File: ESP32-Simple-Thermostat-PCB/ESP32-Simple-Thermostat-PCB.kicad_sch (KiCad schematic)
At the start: 47 parts, among them J1 PINHD_1x18_Male, J2 Screw_Terminal_9_P3.50mm, J3 DS18B20, J4 3.2 lcd tft, K1 G5Q-1A, K2 G5Q-1A, K3 G5Q-1A, K4 G5Q-1A, K5 G5Q-1A, K6 G5Q-1A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

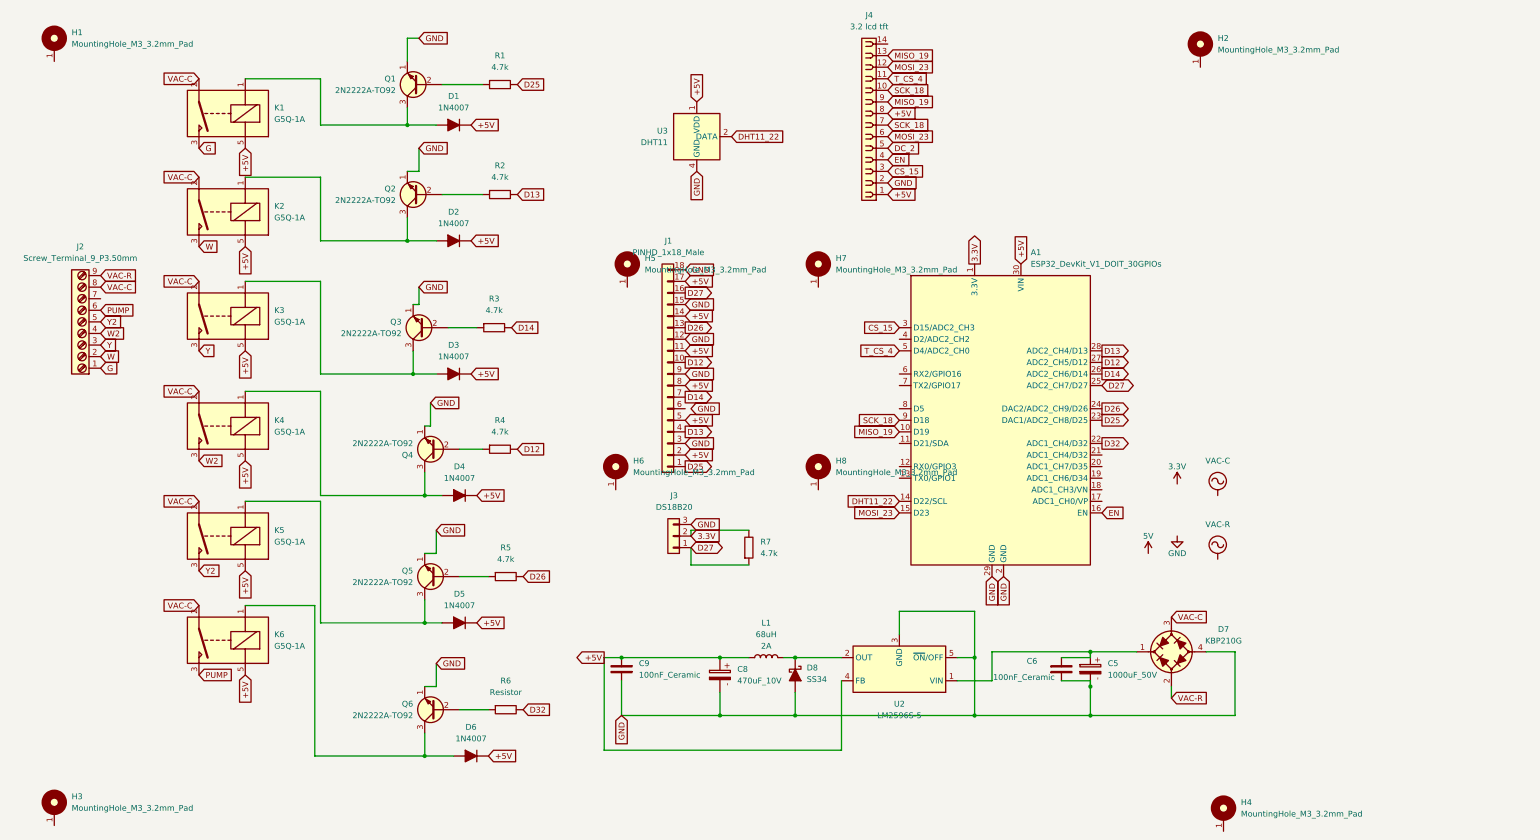
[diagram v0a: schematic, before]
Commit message: Standardize project naming to ESP32 Simple Thermostat
- Updated display text, serial messages, and MQTT device model
- Updated all web interface page titles and headers
- Consistent branding across documentation and code
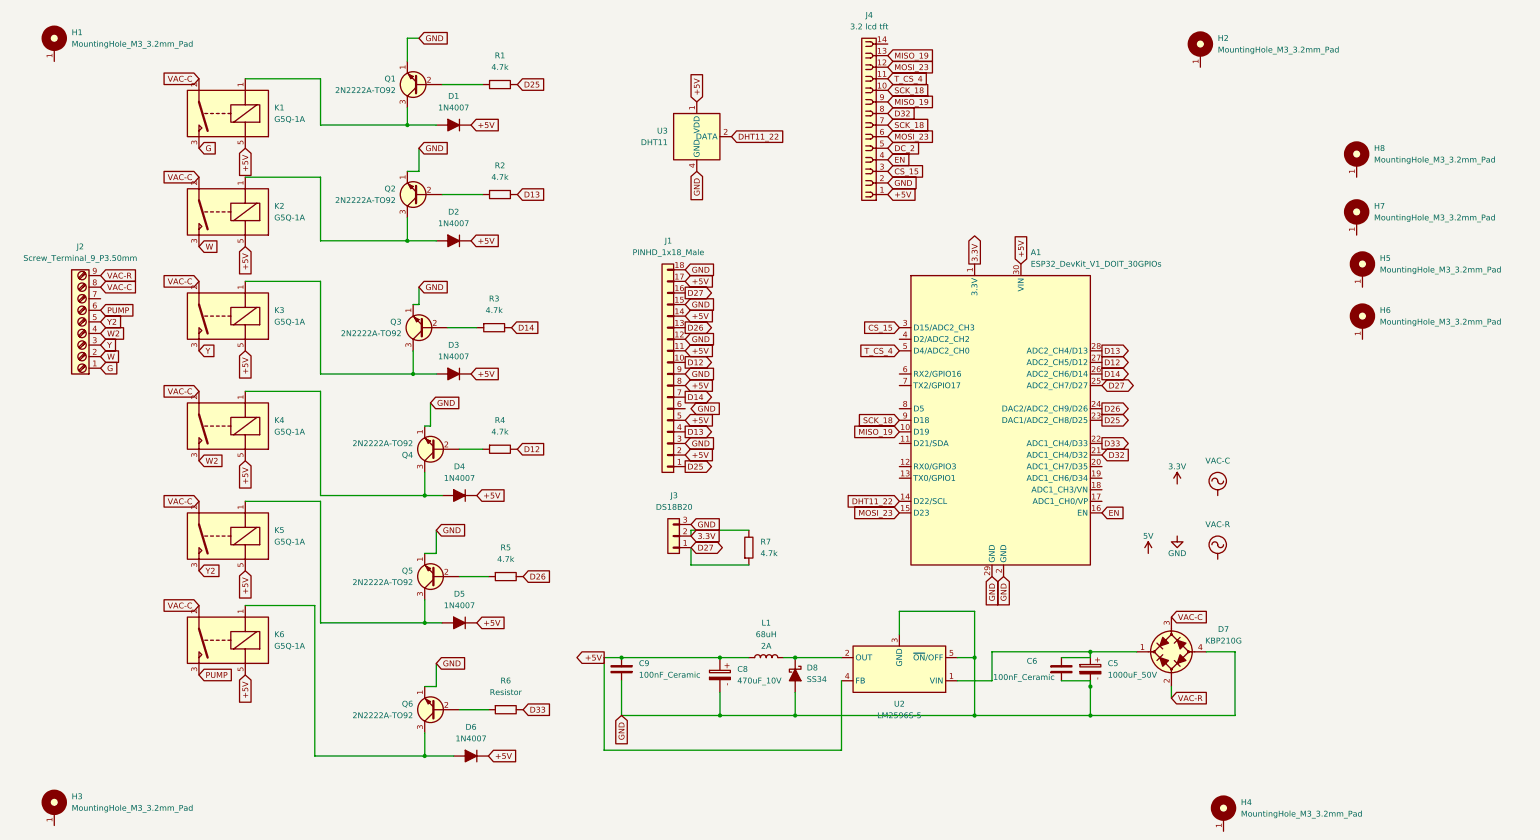
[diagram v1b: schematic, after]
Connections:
- net +5V: no longer J4.8
- net D32: now also A1.21 (ADC1_CH4/D32), J4.8; no longer A1.22 (ADC1_CH4/D32), R6.2
- new net D33: A1.22 (ADC1_CH4/D33), R6.2
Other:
- moved on the sheet: H5, H6, H7, H8
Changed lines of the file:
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@@
 		)
 	)
-	(global_label "+5V"
+	(global_label "D32"
 		(shape input)
-		(at 160.02 90.17 0)
+		(at 251.46 113.03 0)
 		(fields_autoplaced yes)
 		(effects
@@
 		)
 		(property "Intersheetrefs" "${INTERSHEET_REFS}"
-			(at 166.8757 90.17 0)
+			(at 258.1342 113.03 0)
 			(effects
 				(font
@@
 		)
 	)
-	(global_label "D13"
+	(global_label "+5V"
 		(shape input)
-		(at 123.19 55.88 0)
+		(at 160.02 90.17 0)
 		(fields_autoplaced yes)
 		(effects
@@
 		)
 		(property "Intersheetrefs" "${INTERSHEET_REFS}"
-			(at 129.8642 55.88 0)
+			(at 166.8757 90.17 0)
 			(effects
 				(font
@@
 		)
 	)
-	(global_label "+5V"
+	(global_label "D13"
 		(shape input)
-		(at 204.47 38.1 0)
+		(at 123.19 55.88 0)
 		(fields_autoplaced yes)
 		(effects
@@
 		)
 		(property "Intersheetrefs" "${INTERSHEET_REFS}"
-			(at 211.3257 38.1 0)
+			(at 129.8642 55.88 0)
 			(effects
 				(font
@@
 		)
 	)
-	(global_label "D32"
+	(global_label "D33"
 		(shape input)
 		(at 124.46 168.91 0)
@@
 		)
 	)
-	(global_label "D32"
+	(global_label "D33"
 		(shape output)
 		(at 251.46 110.49 0)
@@
 		)
 	)
+	(global_label "D32"
+		(shape input)
+		(at 204.47 38.1 0)
+		(fields_autoplaced yes)
+		(effects
+			(font
+				(size 1.27 1.27)
+			)
+			(justify left)
+		)
+		(property "Intersheetrefs" "${INTERSHEET_REFS}"
+			(at 211.1442 38.1 0)
+			(effects
+				(font
+					(size 1.27 1.27)
+				)
+				(justify left)
+				(hide yes)
+			)
+		)
+	)
 	(global_label "D14"
 		(shape output)
@@
 	(symbol
 		(lib_id "PCM_SL_Mechanical:MountingHole_M3_3.2mm_Pad")
-		(at 147.32 71.12 0)
+		(at 308.61 71.12 0)
 		(unit 1)
 		(exclude_from_sim no)
@@
 		(fields_autoplaced yes)
 		(property "Reference" "H5"
-			(at 151.13 69.8499 0)
+			(at 312.42 69.8499 0)
 			(effects
 				(font
@@
 		)
 		(property "Value" "MountingHole_M3_3.2mm_Pad"
-			(at 151.13 72.3899 0)
+			(at 312.42 72.3899 0)
 			(effects
 				(font
@@
 		)
 		(property "Footprint" "PCM_SL_Mechanical:MountingHole_3.2mm_Pad"
-			(at 147.32 74.93 0)
+			(at 308.61 74.93 0)
 			(effects
 				(font
@@
 		)
 		(property "Datasheet" ""
-			(at 147.32 71.12 0)
+			(at 308.61 71.12 0)
 			(effects
 				(font
@@
 		)
 		(property "Description" "3.2mm Diameter Mounting Hole Pad (M3)"
-			(at 147.32 71.12 0)
+			(at 308.61 71.12 0)
 			(effects
 				(font
@@
 	(symbol
 		(lib_id "PCM_SL_Mechanical:MountingHole_M3_3.2mm_Pad")
-		(at 189.23 115.57 0)
+		(at 307.34 46.99 0)
 		(unit 1)
 		(exclude_from_sim no)
@@
 		(fields_autoplaced yes)
 		(property "Reference" "H8"
-			(at 193.04 114.2999 0)
+			(at 311.15 45.7199 0)
 			(effects
 				(font
@@
 		)
 		(property "Value" "MountingHole_M3_3.2mm_Pad"
-			(at 193.04 116.8399 0)
+			(at 311.15 48.2599 0)
 			(effects
 				(font
@@
 		)
 		(property "Footprint" "PCM_SL_Mechanical:MountingHole_3.2mm_Pad"
-			(at 189.23 119.38 0)
+			(at 307.34 50.8 0)
 			(effects
 				(font
@@
 		)
 		(property "Datasheet" ""
-			(at 189.23 115.57 0)
+			(at 307.34 46.99 0)
 			(effects
 				(font
@@
 		)
 		(property "Description" "3.2mm Diameter Mounting Hole Pad (M3)"
-			(at 189.23 115.57 0)
+			(at 307.34 46.99 0)
 			(effects
 				(font
@@
 	(symbol
 		(lib_id "PCM_SL_Mechanical:MountingHole_M3_3.2mm_Pad")
-		(at 144.78 115.57 0)
+		(at 308.61 82.55 0)
 		(unit 1)
 		(exclude_from_sim no)
@@
 		(fields_autoplaced yes)
 		(property "Reference" "H6"
-			(at 148.59 114.2999 0)
+			(at 312.42 81.2799 0)
 			(effects
 				(font
@@
 		)
 		(property "Value" "MountingHole_M3_3.2mm_Pad"
-			(at 148.59 116.8399 0)
+			(at 312.42 83.8199 0)
 			(effects
 				(font
@@
 		)
 		(property "Footprint" "PCM_SL_Mechanical:MountingHole_3.2mm_Pad"
-			(at 144.78 119.38 0)
+			(at 308.61 86.36 0)
 			(effects
 				(font
@@
 		)
 		(property "Datasheet" ""
-			(at 144.78 115.57 0)
+			(at 308.61 82.55 0)
 			(effects
 				(font
@@
 		)
 		(property "Description" "3.2mm Diameter Mounting Hole Pad (M3)"
-			(at 144.78 115.57 0)
+			(at 308.61 82.55 0)
 			(effects
 				(font
@@
 	(symbol
 		(lib_id "PCM_SL_Mechanical:MountingHole_M3_3.2mm_Pad")
-		(at 189.23 71.12 0)
+		(at 307.34 59.69 0)
 		(unit 1)
 		(exclude_from_sim no)
@@
 		(fields_autoplaced yes)
 		(property "Reference" "H7"
-			(at 193.04 69.8499 0)
+			(at 311.15 58.4199 0)
 			(effects
 				(font
@@
 		)
 		(property "Value" "MountingHole_M3_3.2mm_Pad"
-			(at 193.04 72.3899 0)
+			(at 311.15 60.9599 0)
 			(effects
 				(font
@@
 		)
 		(property "Footprint" "PCM_SL_Mechanical:MountingHole_3.2mm_Pad"
-			(at 189.23 74.93 0)
+			(at 307.34 63.5 0)
 			(effects
 				(font
@@
 		)
 		(property "Datasheet" ""
-			(at 189.23 71.12 0)
+			(at 307.34 59.69 0)
 			(effects
 				(font
@@
 		)
 		(property "Description" "3.2mm Diameter Mounting Hole Pad (M3)"
-			(at 189.23 71.12 0)
+			(at 307.34 59.69 0)
 			(effects
 				(font
